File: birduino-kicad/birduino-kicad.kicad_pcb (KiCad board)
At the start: 2 copper layers, 47.5 x 71.9 mm, 22 parts, among them J1 Conn_01x03_Male, J2 Conn_01x02_Male, J3 Conn_02x05_Odd_Even, J4 Conn_01x04, Q1 2N7000, Q2 2N7000, Q3 2N7000, SW1 SW_Push_Dual, SW2 SW_Push_Dual, SW3 SW_Push_Dual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

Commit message: feat: add new sensors and components
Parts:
- added J10: Conn_01x01_Male, Connector_PinHeader_2.54mm:PinHeader_1x01_P2.54mm_Vertical, F.Cu at (131.8, 103.4)
- added J5: Conn_01x01_Male, Connector_PinHeader_2.54mm:PinHeader_1x01_P2.54mm_Vertical, F.Cu at (139.7, 85.6)
- added J6: Conn_01x01_Male, Connector_PinHeader_2.54mm:PinHeader_1x01_P2.54mm_Vertical, F.Cu at (132.1, 85.6)
- added J7: Conn_01x01_Male, Connector_PinHeader_2.54mm:PinHeader_1x01_P2.54mm_Vertical, F.Cu at (135.9, 85.6)
- added J8: Conn_02x02_Odd_Even, Connector_PinHeader_2.54mm:PinHeader_2x02_P2.54mm_Vertical, F.Cu at (167.1, 85.3)
- added J9: Conn_01x02, Connector_PinHeader_2.54mm:PinHeader_1x02_P2.54mm_Vertical, F.Cu at (131.8, 94.7)
- moved SW3 1.05 mm to (160.0, 93.7)
- moved SW1 0.51 mm to (137.9, 93.5)
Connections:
- Q1 pad 3: (no net) -> Net-(J5-Pad1)
- Q2 pad 3: (no net) -> Net-(J6-Pad1)
- Q3 pad 3: (no net) -> Net-(J7-Pad1)
- U1 pad 12: (no net) -> FREE
- U1 pad 26: (no net) -> PUMP
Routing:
- net VCC: track 0.00 -> 191.1 mm
- net GND: track 0.00 -> 179.7 mm
- net SDA: track 0.00 -> 55.5 mm
- net BT4: track 0.00 -> 54.8 mm
- net TEMP: track 0.00 -> 53.6 mm
- net BT3: track 0.00 -> 52.4 mm
- net SCL: track 0.00 -> 51.3 mm
- net Net-(J1-Pad1): track 0.00 -> 50.9 mm
- net LED2: track 0.00 -> 50.8 mm
- net FREE: track 0.00 -> 44.9 mm
- net Net-(J5-Pad1): track 0.00 -> 37.6 mm
- net BT1: track 0.00 -> 36.6 mm
- net LED1: track 0.00 -> 36.4 mm
- net SCK: track 0.00 -> 34.4 mm
- net Net-(J6-Pad1): track 0.00 -> 32.0 mm
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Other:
- board text added: "F"
- board text added: "G"
- board text added: "LA1"
- board text added: "LA2"
- board text added: "LA3"
- board text added: "P"
- board text added: "birduino 1.0 2018 (c) Designed in Berlin"

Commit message: feat: First final version 1.0. 3D image added to readme
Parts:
- added C1: 0.1uF, Capacitor_THT:C_Disc_D3.0mm_W2.0mm_P2.50mm, F.Cu at (173.0, 105.7)
- added C2: 100uF, Capacitor_THT:CP_Radial_D6.3mm_P2.50mm, F.Cu at (131.8, 120.9)
- added C3: 150uF, Capacitor_THT:C_Radial_D8.0mm_H7.0mm_P3.50mm, F.Cu at (131.6, 111.5)
- added D1: 1N5817, Diode_THT:D_DO-41_SOD81_P7.62mm_Horizontal, F.Cu at (150.1, 147.8)
- added J11: Conn_01x01_Male, Connector_PinHeader_2.54mm:PinHeader_1x01_P2.54mm_Vertical, F.Cu at (172.5, 94.7)
- added L1: 22uH, Inductor_THT:L_Axial_L9.5mm_D4.0mm_P12.70mm_Horizontal_Fastron_SMCC, F.Cu at (155.2, 147.8)
- added U3: MAX756CPA, Package_DIP:DIP-8_W7.62mm, F.Cu at (151.1, 97.8)
- moved R3 18.9 mm to (165.4, 131.8), turned to 180 degrees
- moved R6 18.9 mm to (165.4, 124.2), turned to 180 degrees
- moved R1 18.6 mm to (165.4, 136.9), turned to 180 degrees
- moved R4 18.5 mm to (165.4, 129.3), turned to 180 degrees
- moved R2 18.4 mm to (165.4, 134.4), turned to 180 degrees
- moved R5 18.2 mm to (165.4, 126.7), turned to 180 degrees
- moved Q3 17.8 mm to (152.1, 116.8)
- moved Q2 16.8 mm to (152.4, 124.0)
- moved Q1 16.5 mm to (152.1, 131.1)
- moved R9 15.8 mm to (160.3, 117.1), turned to 0 degrees
- moved R8 14.7 mm to (160.3, 119.4), turned to 0 degrees
- moved R7 14.4 mm to (160.3, 121.7), turned to 0 degrees
- moved U2 6.40 mm to (132.1, 128.0)
- moved J4 3.18 mm to (155.4, 82.8)
- moved SW1 2.17 mm to (140.0, 94.2)
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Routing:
- net /StepUp5V/5V: track 0.00 -> 95.9 mm
- net Net-(D1-Pad2): track 0.00 -> 47.0 mm
- net LED2: track 50.8 -> 21.4 mm
- net GND: track 179.7 -> 208.0 mm
- net VCC: track 191.1 -> 214.9 mm
- net Net-(C1-Pad1): track 0.00 -> 23.7 mm
- net Net-(J6-Pad1): track 32.0 -> 53.6 mm, vias 0 -> 1
- net LED1: track 36.4 -> 18.1 mm
- net Net-(J7-Pad1): track 24.5 -> 42.7 mm, vias 0 -> 1
- net Net-(J5-Pad1): track 37.6 -> 55.5 mm, vias 0 -> 1
- net Net-(J1-Pad1): track 50.9 -> 67.3 mm
- net Net-(J1-Pad3): track 27.8 -> 20.5 mm
- net PUMP: track 31.6 -> 38.5 mm
- net BT4: track 54.8 -> 61.1 mm
- net Net-(J1-Pad2): track 26.9 -> 20.8 mm
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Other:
- board text added: "5V"
- board text added: "birduino 1.0 2019 (c) Designed in Berlin"
- board text removed: "birduino 1.0 2018 (c) Designed in Berlin"

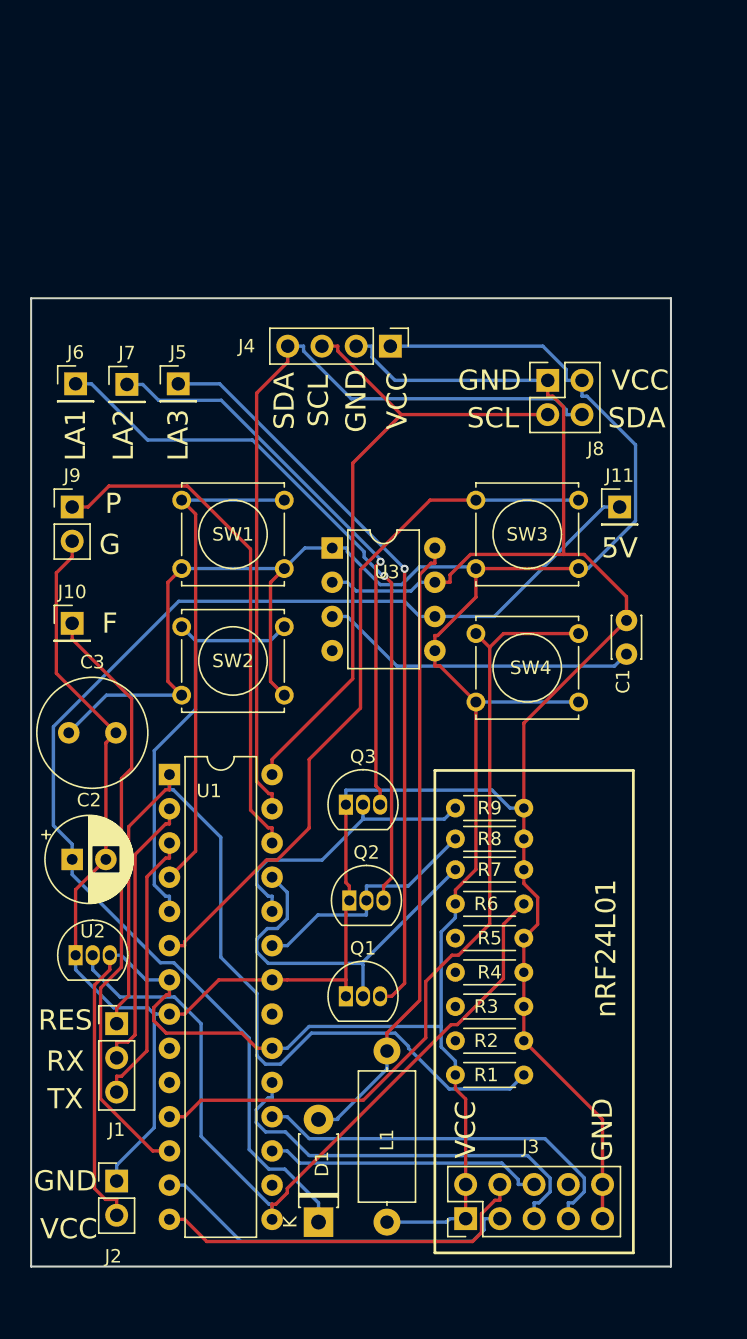
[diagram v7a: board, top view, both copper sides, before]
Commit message: feat: added Crytal to PCB. Added new images to readme.
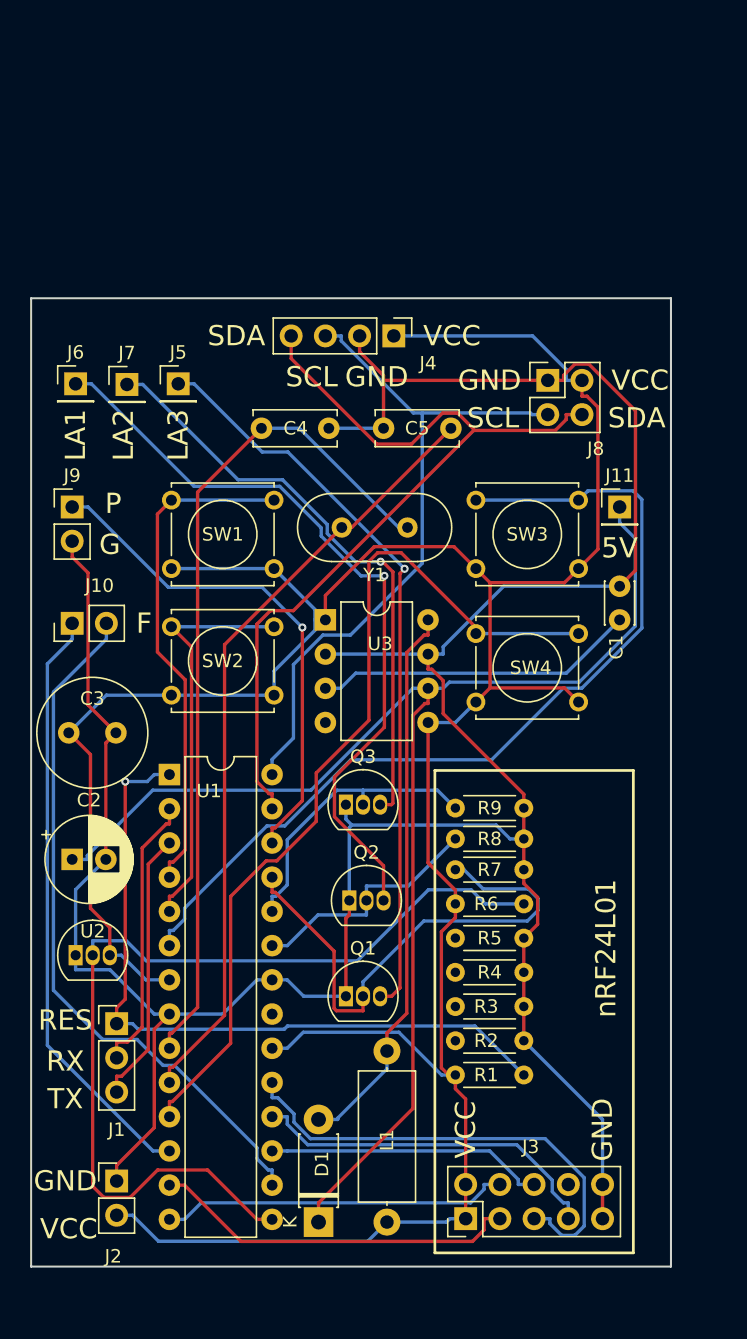
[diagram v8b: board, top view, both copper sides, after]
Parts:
- added C4: 22uF, Capacitor_THT:C_Disc_D6.0mm_W2.5mm_P5.00mm, F.Cu at (145.9, 88.9)
- added C5: 22uF, Capacitor_THT:C_Disc_D6.0mm_W2.5mm_P5.00mm, F.Cu at (154.9, 88.9)
- added Y1: Crystal, Crystal:Crystal_HC49-4H_Vertical, F.Cu at (156.7, 96.3)
- J10: value Conn_01x01_Male -> Conn_01x02_Male; footprint Connector_PinHeader_2.54mm:PinHeader_1x01_P2.54mm_Vertical -> Connector_PinHeader_2.54mm:PinHeader_1x02_P2.54mm_Vertical
- moved U3 5.36 mm to (150.6, 103.1)
- moved C1 2.59 mm to (172.5, 103.1)
- moved J4 0.80 mm to (155.7, 82.0)
- moved SW1 0.76 mm to (139.2, 94.2)
- moved SW2 0.76 mm to (139.2, 103.6)
- turned J10 to 90 degrees
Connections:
- U1 pad 10: (no net) -> XTAL2
- U1 pad 16: (no net) -> FREE2
- U1 pad 9: (no net) -> XTAL1
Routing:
- net XTAL1: track 0.00 -> 62.9 mm
- net XTAL2: track 0.00 -> 57.8 mm
- net FREE2: track 0.00 -> 52.2 mm
- net BT3: track 53.2 -> 68.4 mm
- net Net-(J1-Pad1): track 67.3 -> 53.7 mm, vias 0 -> 1
- net LED3: track 27.8 -> 39.2 mm
- net TEMP: track 59.2 -> 69.5 mm
- net GND: track 208.0 -> 217.8 mm
- net /StepUp5V/5V: track 95.9 -> 101.6 mm
- net Net-(D1-Pad2): track 47.0 -> 41.5 mm
- net BT4: track 61.1 -> 66.5 mm
- net SCK: track 30.9 -> 35.4 mm
- net SDA: track 60.3 -> 64.5 mm
- net Net-(J6-Pad1): track 53.6 -> 56.3 mm
- net CSN: track 28.5 -> 25.8 mm
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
